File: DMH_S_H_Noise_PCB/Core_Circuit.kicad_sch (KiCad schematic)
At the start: 0 parts

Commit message: Started schematic
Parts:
- added U1: TL074, Package_DIP:DIP-14_W7.62mm_Socket, symbol Amplifier_Operational:TL074

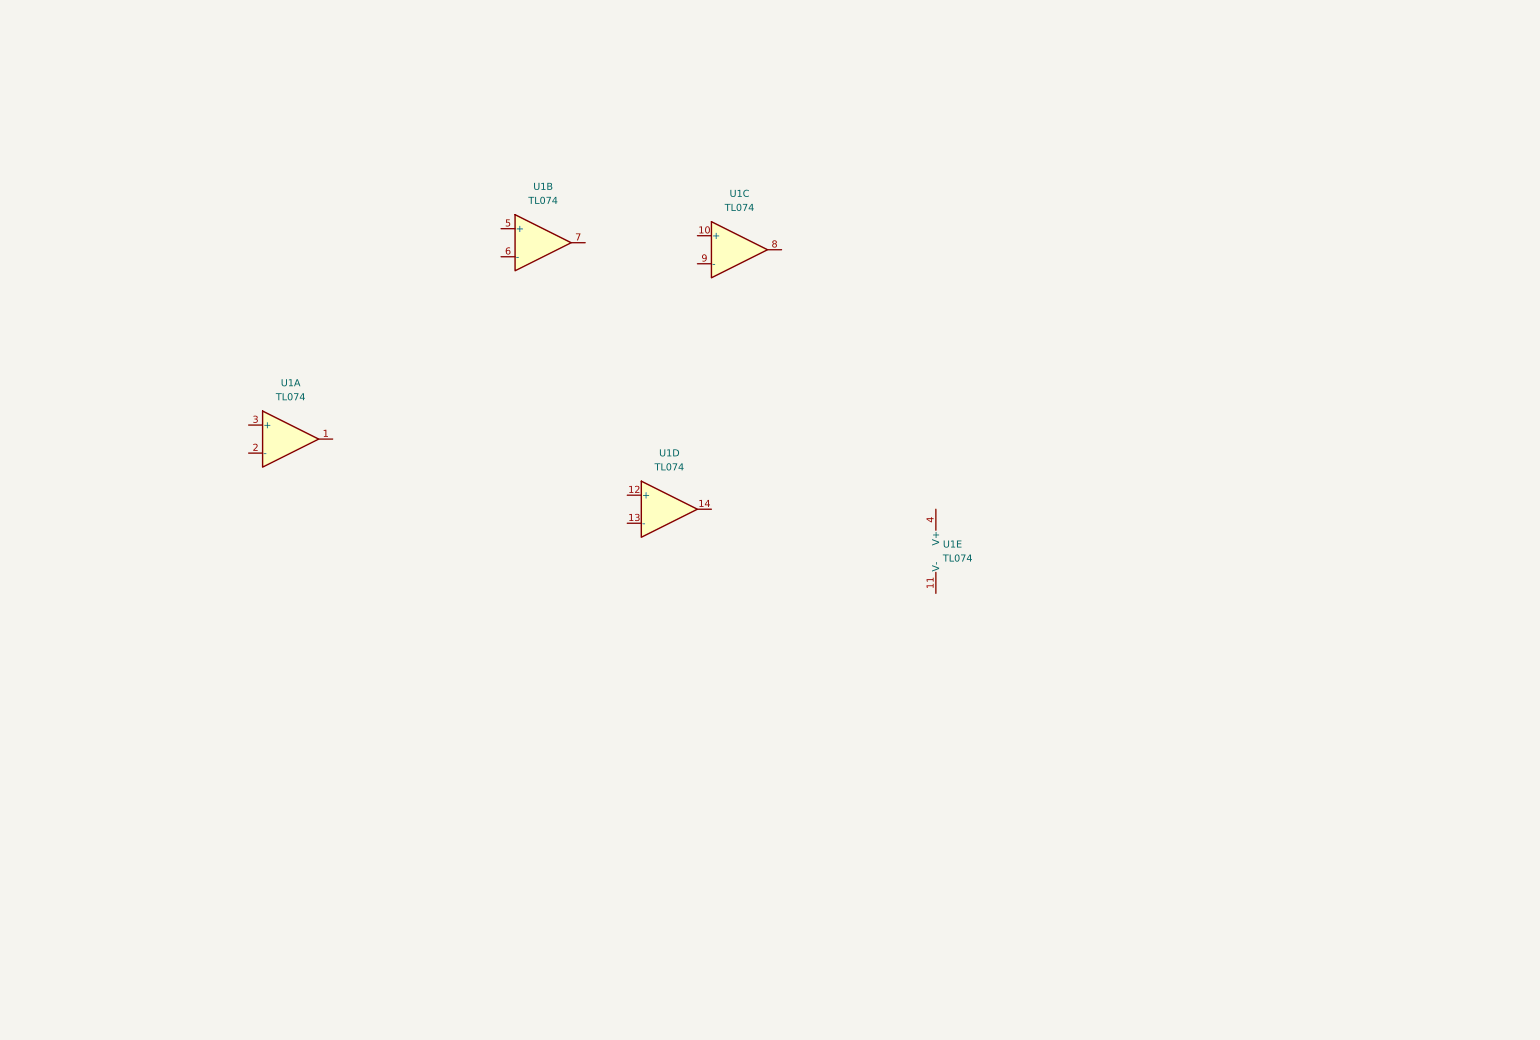
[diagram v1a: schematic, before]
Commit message: Designed S&h circuit
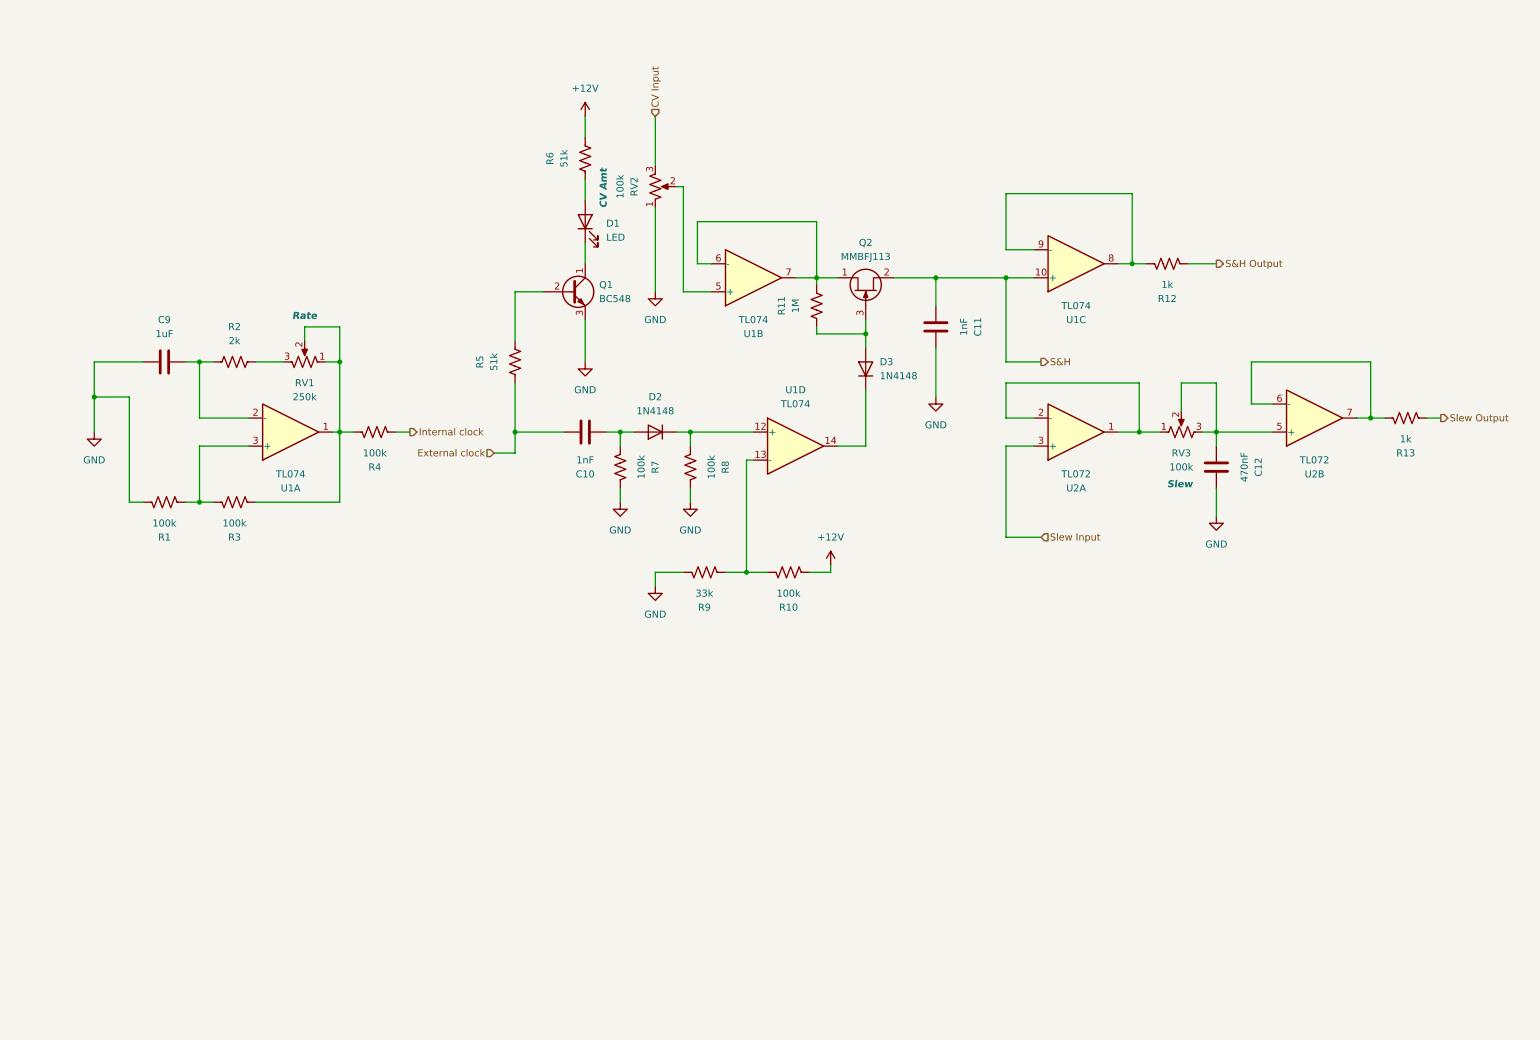
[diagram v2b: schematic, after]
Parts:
- removed unit 5 of U1
- added C10, C11: 1nF, Capacitor_THT:C_Disc_D4.3mm_W1.9mm_P5.00mm, symbol Device:C
- added C12: 470nF, Capacitor_THT:C_Disc_D4.3mm_W1.9mm_P5.00mm, symbol Device:C
- added C9: 1uF, Capacitor_THT:C_Disc_D4.3mm_W1.9mm_P5.00mm, symbol Device:C
- added D1: LED, LED_THT:LED_D3.0mm, symbol Device:LED
- added D2, D3: 1N4148, Diode_THT:D_DO-35_SOD27_P7.62mm_Horizontal, symbol Device:D
- added Q1: BC548, Package_TO_SOT_THT:TO-92_Inline_Wide, symbol Transistor_BJT:BC548
- added Q2: MMBFJ113, Package_TO_SOT_SMD:SOT-23, symbol Transistor_FET:MMBFJ113
- added R1, R10, R3, R4, R7, R8: 100k, Resistor_THT:R_Axial_DIN0207_L6.3mm_D2.5mm_P7.62mm_Horizontal, symbol Device:R_US
- added R11: 1M, Resistor_THT:R_Axial_DIN0207_L6.3mm_D2.5mm_P7.62mm_Horizontal, symbol Device:R_US
- added R12, R13: 1k, Resistor_THT:R_Axial_DIN0207_L6.3mm_D2.5mm_P7.62mm_Horizontal, symbol Device:R_US
- added R2: 2k, Resistor_THT:R_Axial_DIN0207_L6.3mm_D2.5mm_P7.62mm_Horizontal, symbol Device:R_US
- added R5, R6: 51k, Resistor_THT:R_Axial_DIN0207_L6.3mm_D2.5mm_P7.62mm_Horizontal, symbol Device:R_US
- added R9: 33k, Resistor_THT:R_Axial_DIN0207_L6.3mm_D2.5mm_P7.62mm_Horizontal, symbol Device:R_US
- added RV1: 250k, Potentiometer_THT:Potentiometer_Alpha_RD901F-40-00D_Single_Vertical, symbol Device:R_Potentiometer_US
- added RV2, RV3: 100k, Potentiometer_THT:Potentiometer_Alpha_RD901F-40-00D_Single_Vertical, symbol Device:R_Potentiometer_US
- added U2: TL072, Package_DIP:DIP-8_W7.62mm_Socket, symbol Amplifier_Operational:TL072
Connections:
- net at U1.5 (+): now also RV2.2
- net at U1.6 (-): now also U1.7, Q2.1 (D), R11.1
- net at U1.1: now also R3.1, R4.2, RV1.1, RV1.2
- net at U1.2 (-): now also C9.2, R2.2
- net at U1.3 (+): now also R1.1, R3.2
- net at U1.12 (+): now also D2.1 (K), R8.1
- net at U1.13 (-): now also R10.2, R9.1
- net at U1.14: now also D3.1 (K)
- net S&H: now reaches U1.10 (+)
- net S&H: now also C11.1, Q2.2 (S)
- net at U1.8: now also U1.9 (-), R12.2
- new net: D1.1 (K), Q1.1 (C)
- new net: D1.2 (A), R6.2
- new net: RV3.1, U2.1, U2.2 (-)
- new net: C12.1, RV3.2, RV3.3, U2.5 (+)
- new net: R13.2, U2.6 (-), U2.7
- new net: C10.1, D2.2 (A), R7.1
- new net: Q1.2 (B), R5.1
- new net: D3.2 (A), Q2.3 (G), R11.2
- new net: R2.1, RV1.3
- new net +12V: R10.1, R6.1
- new net CV Input: RV2.3
- new net External clock: C10.2, R5.2
- new net GND: C11.2, C12.2, C9.1, Q1.3 (E), R1.2, R7.2, R8.2, R9.2, RV2.1
- new net Internal clock: R4.1
- new net S&H Output: R12.1
- new net Slew Input: U2.3 (+)
- new net Slew Output: R13.1
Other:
- moved on the sheet: U1A, U1B, U1C, U1D

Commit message: Completed circuit
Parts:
- added C13: 1uF, Capacitor_THT:C_Disc_D4.3mm_W1.9mm_P5.00mm, symbol Device:C
- added C14, C17: 680pF, Capacitor_THT:C_Disc_D4.3mm_W1.9mm_P5.00mm, symbol Device:C
- added C15, C18: 2.2nF, Capacitor_THT:C_Disc_D4.3mm_W1.9mm_P5.00mm, symbol Device:C
- added C16, C19: 5.6nF, Capacitor_THT:C_Disc_D4.3mm_W1.9mm_P5.00mm, symbol Device:C
- added Q3: BC548, Package_TO_SOT_THT:TO-92_Inline_Wide, symbol Transistor_BJT:BC548
- added R14, R15, R17, R19, R24, R30, R37: 100k, Resistor_THT:R_Axial_DIN0207_L6.3mm_D2.5mm_P7.62mm_Horizontal, symbol Device:R_US
- added R16: 680R, Resistor_THT:R_Axial_DIN0207_L6.3mm_D2.5mm_P7.62mm_Horizontal, symbol Device:R_US
- added R18, R25, R32, R34, R36: 1k, Resistor_THT:R_Axial_DIN0207_L6.3mm_D2.5mm_P7.62mm_Horizontal, symbol Device:R_US
- added R20: 4k7, Resistor_THT:R_Axial_DIN0207_L6.3mm_D2.5mm_P7.62mm_Horizontal, symbol Device:R_US
- added R21: 47k, Resistor_THT:R_Axial_DIN0207_L6.3mm_D2.5mm_P7.62mm_Horizontal, symbol Device:R_US
- added R22, R27: 470k, Resistor_THT:R_Axial_DIN0207_L6.3mm_D2.5mm_P7.62mm_Horizontal, symbol Device:R_US
- added R23: 22k, Resistor_THT:R_Axial_DIN0207_L6.3mm_D2.5mm_P7.62mm_Horizontal, symbol Device:R_US
- added R26: 1M, Resistor_THT:R_Axial_DIN0207_L6.3mm_D2.5mm_P7.62mm_Horizontal, symbol Device:R_US
- added R28: 10k, Resistor_THT:R_Axial_DIN0207_L6.3mm_D2.5mm_P7.62mm_Horizontal, symbol Device:R_US
- added R29: 20k, Resistor_THT:R_Axial_DIN0207_L6.3mm_D2.5mm_P7.62mm_Horizontal, symbol Device:R_US
- added R31: 33k, Resistor_THT:R_Axial_DIN0207_L6.3mm_D2.5mm_P7.62mm_Horizontal, symbol Device:R_US
- added R33, R35: 3k3, Resistor_THT:R_Axial_DIN0207_L6.3mm_D2.5mm_P7.62mm_Horizontal, symbol Device:R_US
- added SW1: SW_Push, symbol Switch:SW_Push
- added U3: TL074, Package_DIP:DIP-14_W7.62mm_Socket, symbol Amplifier_Operational:TL074
- C11: value 1nF -> 100nF
- RV2: Function CV Amt -> Input Level
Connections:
- net +12V: now also R14.1, R35.1, R37.2
- net External clock: now also SW1.2
- net GND: now also Q3.2 (B), R15.2, R16.2, R20.2, R21.2, R22.2, R23.2, R29.2, R30.2, R34.2
- net at R3.1, R4.2, RV1.1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: now also R33.1
- net CV Input renamed Input
- new net: C13.1, Q3.3 (E), R14.2
- new net: R17.1, R18.2, R19.2, U3.1
- new net: R16.1, R17.2, U3.2 (-)
- new net: C13.2, R15.1, U3.3 (+)
- new net: R31.2, R32.2, U3.8
- new net: R33.2, R34.1, R35.2, U3.12 (+)
- new net: R36.1, U3.13 (-), U3.14
- new net: C14.1, C15.1, C16.1, C17.1, C18.1, C19.1, R19.1, U3.5 (+)
- new net: C19.2, R26.2
- new net: R26.1, R27.1, R28.1, R29.1, U3.10 (+)
- new net: C18.2, R27.2
- new net: C15.2, R21.1
- new net: R37.1, SW1.1
- new net: C17.2, R28.2
- new net: C14.2, R20.1
- new net: C16.2, R22.1
- new net: R23.1, R24.1, U3.6 (-)
- new net: R30.1, R31.1, U3.9 (-)
- new net: R24.2, R25.2, U3.7
- new net Blue: R32.1
- new net Clock Out: R36.2
- new net Pink: R25.1
- new net White: R18.1
- no-connect marks 0 -> 1
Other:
- moved on the sheet: C10, C11, C12, C9, D1, D2, D3, Q1, Q2, R1, R10, R11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
